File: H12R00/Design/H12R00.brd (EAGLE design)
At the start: 34.6 x 30 mm, 35 parts, among them P1 HEXABIT_17.32_NO_P3_P6, U1 STM32F091CBU6, U2 AD628ARZ, U3 REF193GSZ, X1 XTALL_CSTCE8M00G52

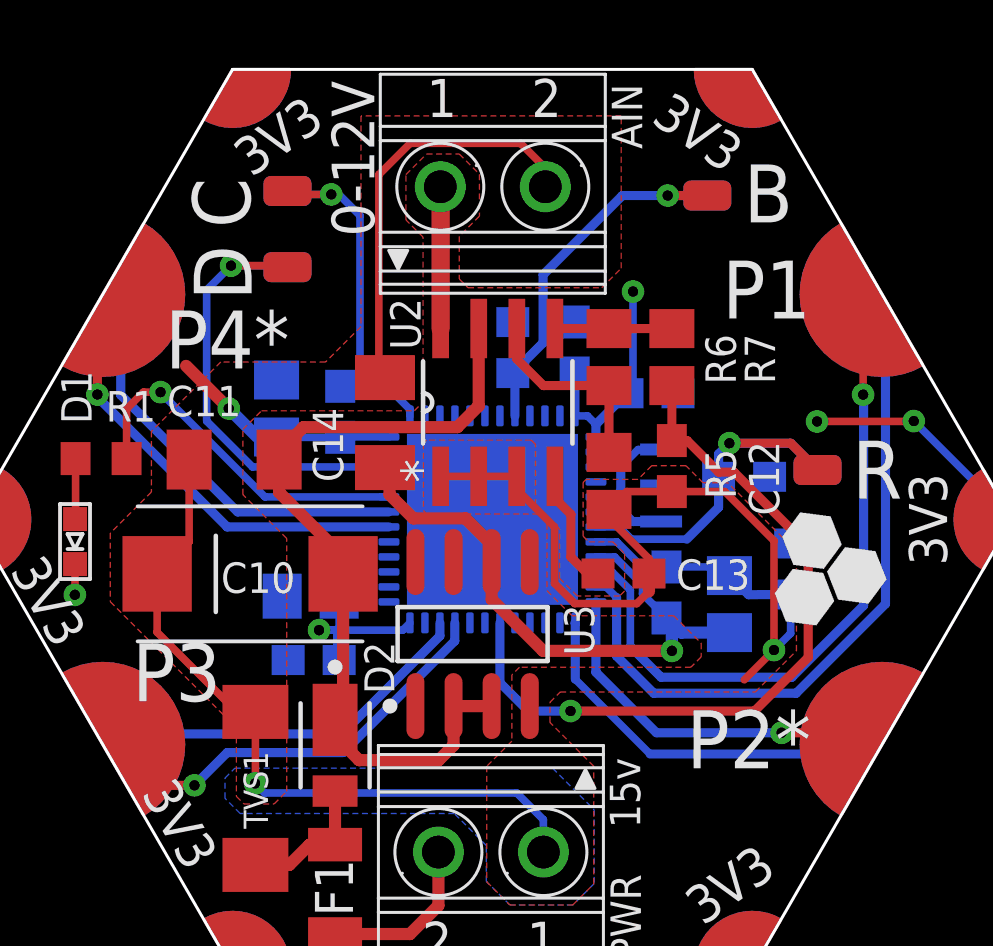
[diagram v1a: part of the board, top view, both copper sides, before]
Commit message: - Fixed labels in .sch and .brd from 12v to 10v - Regenerated docoument file - Fixed BOM - Regenerated output files (Gerber, drills, mount)
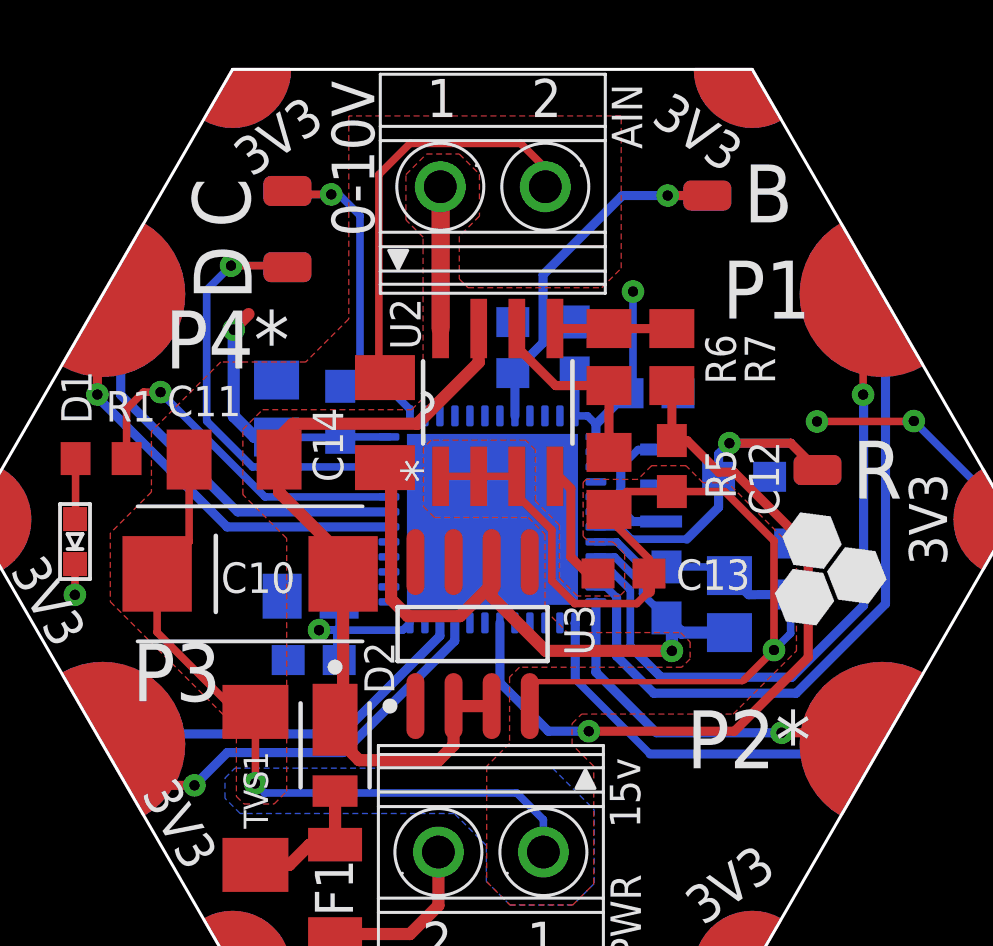
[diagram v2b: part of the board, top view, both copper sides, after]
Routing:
- net VSSA: track 72.2 -> 80.1 mm
- net 3V0: track 20.5 -> 24.0 mm
- net VDD: track 21.8 -> 23.1 mm
- net +15V: track 27.4 -> 26.8 mm
- net AI: track 24.9 -> 25.5 mm
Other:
- board text added: "0-10V"
- board text removed: "0-12V"

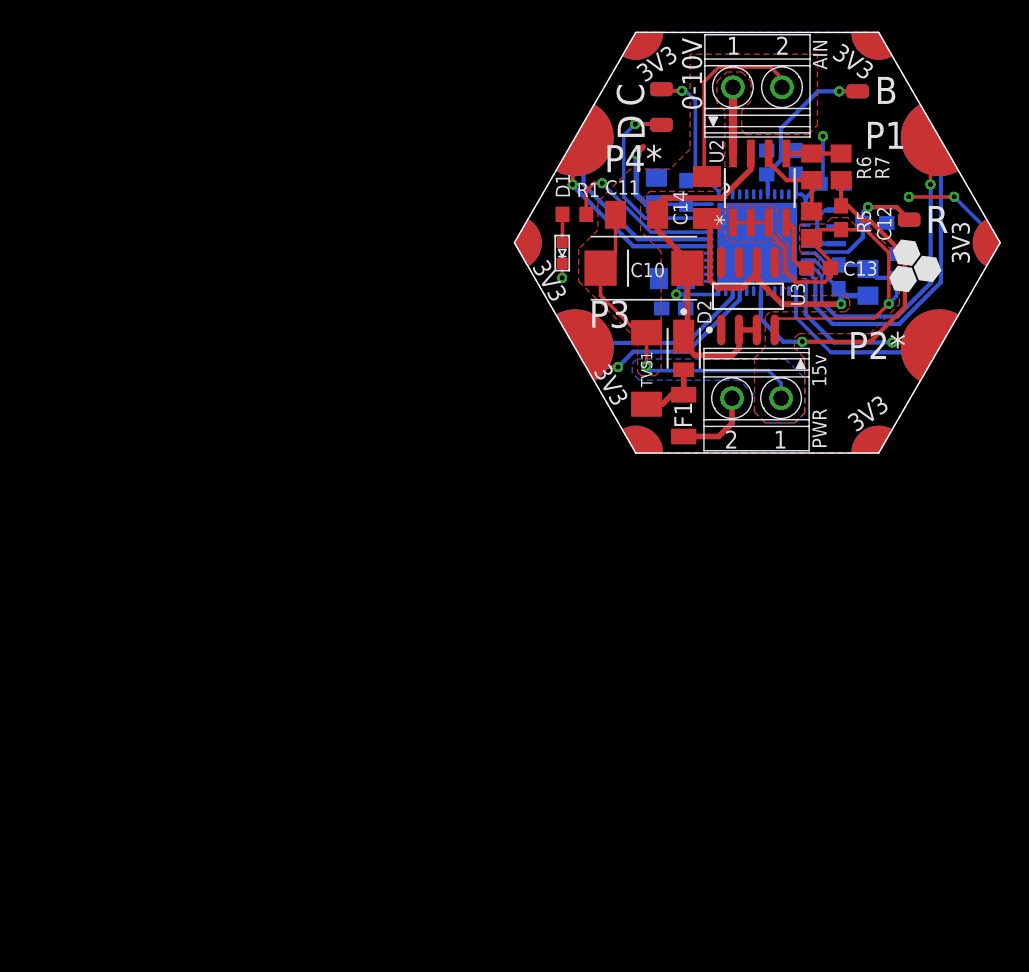
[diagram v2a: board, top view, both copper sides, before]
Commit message: - Made some Hardware modifications (.sch and .brd where updated) - Updated Documentation - Updated BOM - Regenerated output files
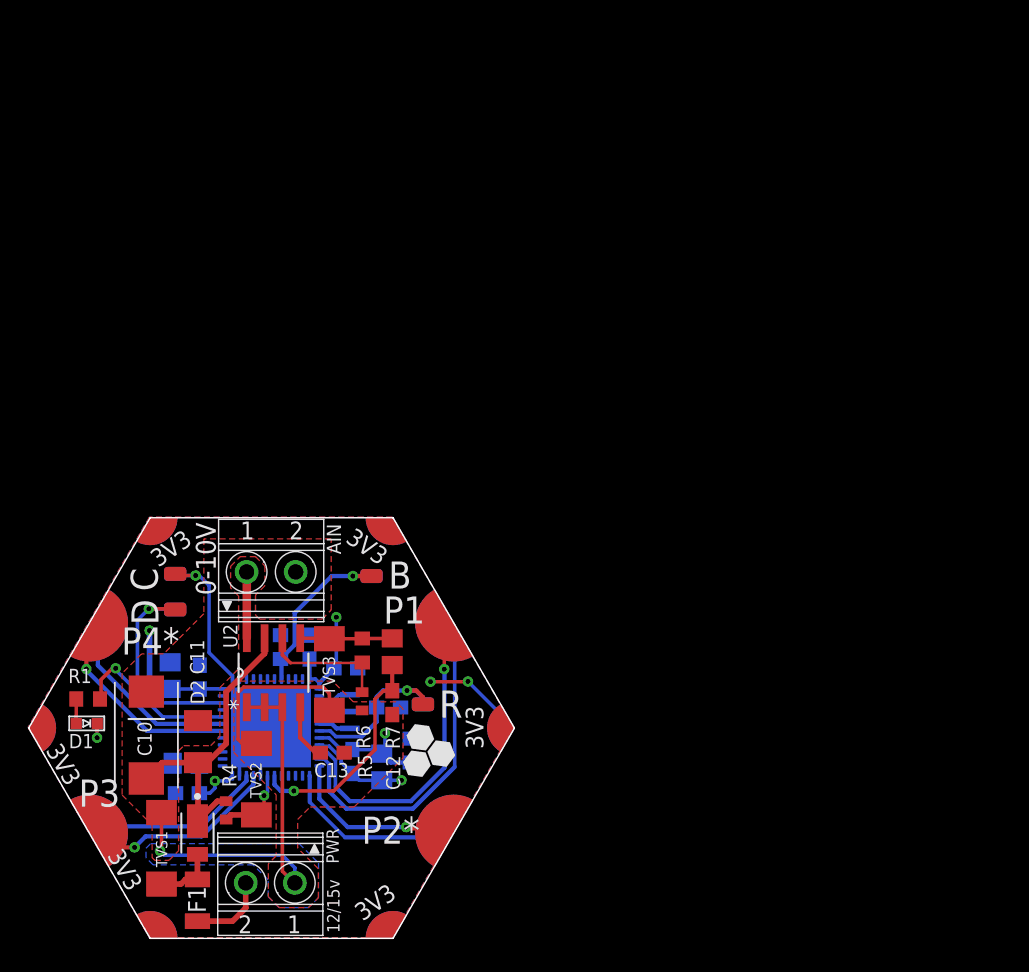
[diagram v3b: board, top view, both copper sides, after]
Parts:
- removed C14: 100 nF, Hexabitz:C1206K
- removed U3: REF193GSZ, Hexabitz:REF193GSZ_1
- added R4: 62k, HEXABITZ_RCLS:R-0402
- added TVS2, TVS3: SMBJ3V3, HEXABITZ_RCLS:DO214AA
- R5: value 10 kΩ -> 51 kΩ; device Hexabitz:R-0805 -> HEXABITZ_RCLS:R-0402
- R6: value 15 kΩ -> 22 kΩ; device Hexabitz:R-0805 -> HEXABITZ_RCLS:R-0603
- moved P1 49.0 mm to (-0.02, 0.00)
- moved AIN 49.0 mm to (-0.05, 11.2)
- moved B 49.0 mm to (7.10, 10.8)
- moved C 49.0 mm to (-6.90, 11.0)
- moved C13 49.0 mm to (4.31, -1.75)
- moved C2 49.0 mm to (7.84, -2.77)
- moved C4 49.0 mm to (-6.12, -2.51)
- moved C5 49.0 mm to (-5.14, 3.64)
- moved C6 49.0 mm to (-6.02, -4.64)
- moved C7 49.0 mm to (-7.26, 3.75)
- moved C9 49.0 mm to (5.27, 4.26)
- moved D 49.0 mm to (-6.90, 8.46)
- moved D2 49.0 mm to (-5.31, -7.48)
- moved F1 49.0 mm to (-5.31, -12.3)
- moved PWR 49.0 mm to (-0.11, -11.1)
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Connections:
- removed net 3V0: C1.1, C14.1, C2.1, U1.P$9, U3.6
- removed net UART6_RX: U1.P$15
- removed net UART6_TX: U1.P$14
- new net AGND: TVS2.A, TVS3.A
- new net VOLTAGE_SCALE: R4.1, TVS2.C, U1.P$19
- net +15V: now also R4.2; no longer U3.2, U3.3
- net GND: now also U1.P$14
- net N$1: now also TVS3.C
- net VDD: now also C1.1, C2.1, U1.P$9
- net VSSA: no longer C14.2, U3.4
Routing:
- net VSSA: track 80.1 -> 38.2 mm
- net 3V0: track 24.0 -> 0.00 mm, vias 1 -> 0
- net AGND: track 0.00 -> 12.8 mm
- net AI: track 25.5 -> 16.1 mm
- net GND: track 8.56 -> 16.2 mm
- net VDD: track 23.1 -> 29.2 mm, vias 3 -> 4
- net VOLTAGE_SCALE: track 0.00 -> 5.74 mm, vias 0 -> 1
- net +15V: track 26.8 -> 22.2 mm
- net N$2: track 6.45 -> 9.25 mm
- net N$1: track 3.90 -> 6.59 mm
- net R1: track 13.6 -> 12.5 mm
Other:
- board text added: "0-10v"
- board text added: "12/15v"
- board text removed: "0-12v"
